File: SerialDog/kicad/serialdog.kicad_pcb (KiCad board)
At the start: 2 copper layers, 4 parts, among them J1 Connector:USB_C_Receptacle, U1 SP0503BAHT, U2 Interface_USB:CP2102N-A01-GQF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

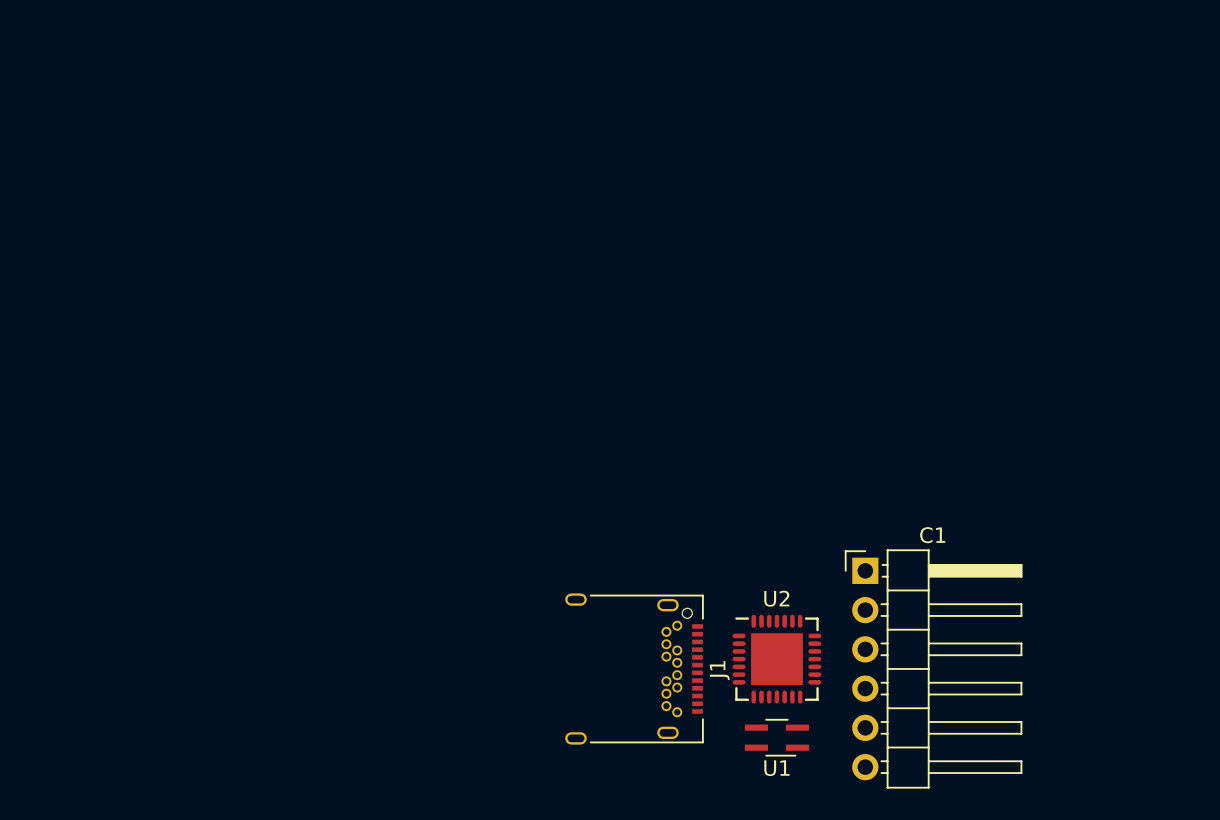
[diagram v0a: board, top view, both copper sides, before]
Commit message: Kicad v5, pcb design started
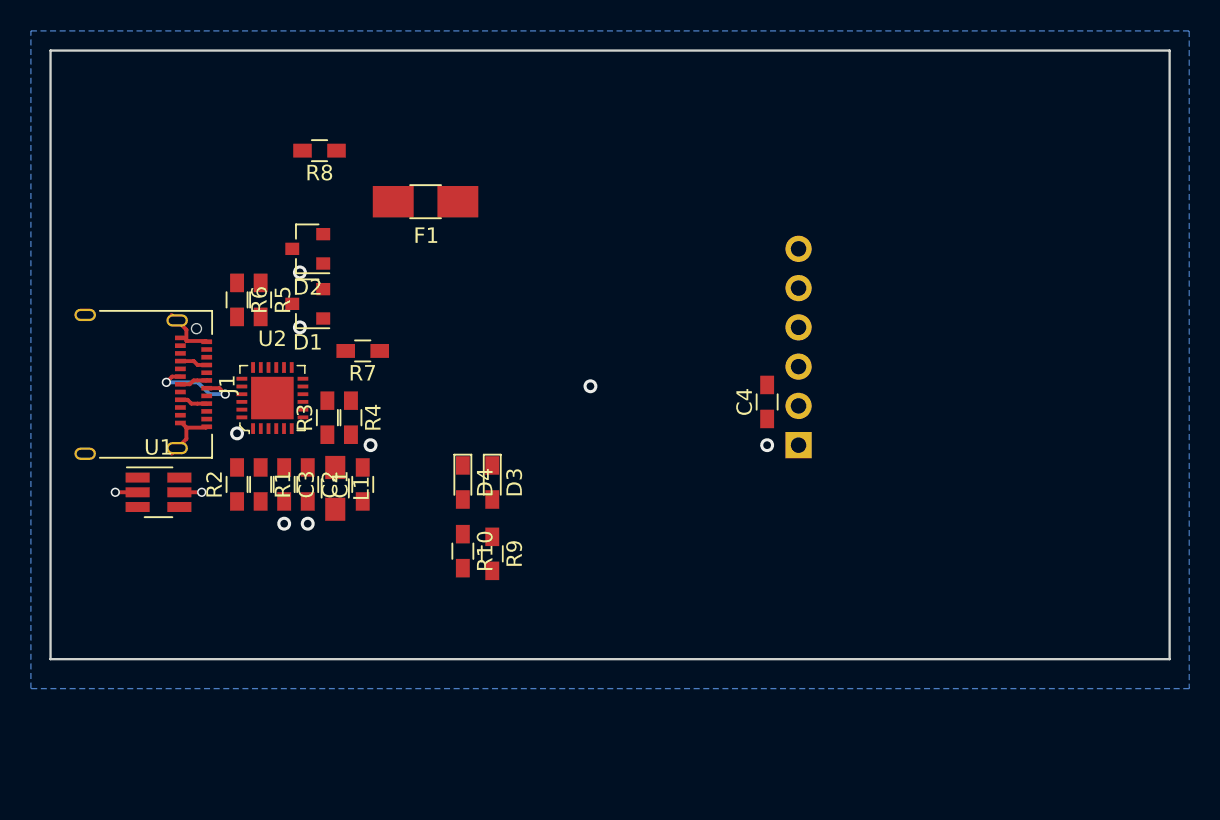
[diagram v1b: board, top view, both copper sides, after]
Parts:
- added C2: 1u, Resistors_SMD:R_0603_HandSoldering, F.Cu at (126.5, 94.7)
- added C3: 1u, Resistors_SMD:R_0603_HandSoldering, F.Cu at (125.0, 94.7)
- added C4: 1u, Resistors_SMD:R_0603_HandSoldering, F.Cu at (156.2, 89.4)
- added D1: BAT54S, TO_SOT_Packages_SMD:SOT-23, F.Cu at (126.5, 83.1)
- added D2: BAT54S, TO_SOT_Packages_SMD:SOT-23, F.Cu at (126.5, 79.5)
- added D3: LED, LEDs:LED_0603_HandSoldering, F.Cu at (138.4, 94.6)
- added D4: LED, LEDs:LED_0603_HandSoldering, F.Cu at (136.5, 94.6)
- added F1: Polyfuse_Small, Fuse_Holders_and_Fuses:Fuse_SMD1206_HandSoldering, F.Cu at (134.1, 76.5)
- added J2: 1x6_2.54_smd_header, Pin_Headers:Pin_Header_Angled_1x06_Pitch2.54mm, B.Cu at (158.2, 92.2)
- added L1: Ferrite_Bead, Resistors_SMD:R_0805_HandSoldering, F.Cu at (128.3, 95.0)
- added R1: 22, Resistors_SMD:R_0603_HandSoldering, F.Cu at (123.4, 94.7)
- added R10: 1k, Resistors_SMD:R_0603_HandSoldering, F.Cu at (136.5, 99.1)
- added R2: 22, Resistors_SMD:R_0603_HandSoldering, F.Cu at (121.9, 94.7)
- added R3: 22k, Resistors_SMD:R_0603_HandSoldering, F.Cu at (127.8, 90.4)
- added R4: 47k, Resistors_SMD:R_0603_HandSoldering, F.Cu at (129.3, 90.4)
- added R5: 22, Resistors_SMD:R_0603_HandSoldering, F.Cu at (123.4, 82.8)
- added R6: 22, Resistors_SMD:R_0603_HandSoldering, F.Cu at (121.9, 82.8)
- added R7: 22, Resistors_SMD:R_0603_HandSoldering, F.Cu at (130.0, 86.1)
- added R8: 22, Resistors_SMD:R_0603_HandSoldering, F.Cu at (127.3, 73.2)
- added R9: 1k, Resistors_SMD:R_0603_HandSoldering, F.Cu at (138.4, 99.2)
- C1: value 1x6_2.54_smd_header -> 1u; footprint Pin_Headers:Pin_Header_Angled_1x06_Pitch2.54mm -> Resistors_SMD:R_0603_HandSoldering
- J1: footprint Connectors_USB:USB_C_Receptacle_Amphenol_12401548E4-2A -> digikey-footprints:USB_C_Receptacle_Amphenol_12401610E4-2A
- U1: value SP0503BAHT -> USBLC6-2SC6; footprint TO_SOT_Packages_SMD:SOT-343_SC-70-4_Handsoldering -> TO_SOT_Packages_SMD:SOT-23-6_Handsoldering
- U2: footprint Housings_DFN_QFN:QFN-28-1EP_5x5mm_Pitch0.5mm -> digikey-footprints:WQFN-24-1EP_4x4mm
- moved U1 43.0 mm to (116.8, 95.2), turned to 0 degrees
- moved U2 36.8 mm to (124.2, 89.2)
- moved J1 36.7 mm to (114.9, 88.3)
- moved C1 33.0 mm to (130.0, 94.7), turned to 90 degrees
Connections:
- C1 pad 1: GND -> /VBUS
- C1 pad 2: Net-(C1-Pad2) -> GND
- J1 pad A4: VCC -> /VBUS
- J1 pad A9: VCC -> /VBUS
- J1 pad B4: VCC -> /VBUS
- J1 pad B6: Net-(J1-PadB6) -> Net-(J1-PadA6)
- J1 pad B7: Net-(J1-PadB7) -> Net-(J1-PadA7)
- J1 pad B9: VCC -> /VBUS
- U1 pad 1: VCC -> Net-(J1-PadA6)
- U1 pad 2: Net-(J1-PadA6) -> GND
- U1 pad 3: Net-(J1-PadB7) -> Net-(J1-PadA7)
- U1 pad 4: GND -> Net-(R1-Pad2)
- U2 pad 20: Net-(C1-Pad4) -> Net-(R5-Pad2)
- U2 pad 21: Net-(C1-Pad5) -> Net-(R6-Pad2)
- U2 pad 3: Net-(J1-PadA6) -> Net-(R2-Pad2)
- U2 pad 4: Net-(J1-PadB7) -> Net-(R1-Pad1)
- U2 pad 5: VCC -> Net-(C3-Pad1)
- U2 pad 6: VCC -> Net-(C3-Pad1)
- U2 pad 7: Net-(U2-Pad7) -> /REGIN
- U2 pad 8: VCC -> Net-(R3-Pad2)
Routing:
- net GND: track 0.00 -> 8.79 mm, vias 0 -> 9
- net Net-(J1-PadA7): track 0.00 -> 6.55 mm, vias 0 -> 2
- net /VBUS: track 0.00 -> 5.05 mm, vias 0 -> 1
- net Net-(J1-PadA6): track 0.00 -> 1.84 mm
- added copper zone on B.Cu, net GND
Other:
- board outline added: 72.4 x 39.4 mm

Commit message: Made first pcb layout draft
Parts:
- C3: footprint Resistors_SMD:R_0603_HandSoldering -> Capacitors_SMD:C_0805
- D3, D4: footprint LEDs:LED_0603_HandSoldering -> LEDs:LED_0603
- J2: footprint Pin_Headers:Pin_Header_Angled_1x06_Pitch2.54mm -> uart-adapters:1x6 header female smd; moved to F.Cu
- R1, R10, R2, R3, R4, R5, R6, R7, R8, R9: footprint Resistors_SMD:R_0603_HandSoldering -> Resistors_SMD:R_0603
- moved C4 23.0 mm to (133.6, 85.0), turned to 0 degrees
- moved J2 21.1 mm to (137.2, 92.5)
- moved R9 14.4 mm to (129.0, 88.3), turned to 180 degrees
- moved R8 13.5 mm to (130.4, 86.2)
- moved F1 13.2 mm to (134.5, 89.7), turned to 90 degrees
- moved R10 12.1 mm to (129.0, 89.5), turned to 180 degrees
- moved D3 9.25 mm to (131.7, 88.3), turned to 180 degrees
- moved J1 8.13 mm to (122.0, 92.2)
- moved U2 7.30 mm to (130.4, 93.0)
- moved R3 7.19 mm to (133.6, 94.6)
- moved D4 7.01 mm to (131.7, 89.5), turned to 180 degrees
- moved R4 6.98 mm to (134.9, 94.6)
- moved D2 6.67 mm to (124.1, 85.7), turned to 0 degrees
- moved C2 6.67 mm to (130.8, 99.8), turned to 180 degrees
- moved C1 6.45 mm to (135.3, 98.6)
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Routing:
- net /VBUS: track 5.05 -> 31.4 mm, vias 1 -> 4
- net Net-(C3-Pad1): track 0.00 -> 20.9 mm, vias 0 -> 4
- net GND: track 8.79 -> 28.1 mm, vias 9 -> 6
- net Net-(R6-Pad2): track 0.00 -> 17.4 mm, vias 0 -> 2
- net /REGIN: track 0.00 -> 16.7 mm, vias 0 -> 2
- net Net-(J2-Pad4): track 0.00 -> 16.6 mm, vias 0 -> 2
- net Net-(J2-Pad5): track 0.00 -> 15.3 mm, vias 0 -> 2
- net Net-(R5-Pad2): track 0.00 -> 14.0 mm, vias 0 -> 2
- net /VOUT: track 0.00 -> 13.1 mm
- net Net-(J1-PadA7): track 6.55 -> 15.0 mm, vias 2 -> 3
- net /TX: track 0.00 -> 8.41 mm
- net Net-(J1-PadA6): track 1.84 -> 10.2 mm
- net /RX: track 0.00 -> 7.73 mm, vias 0 -> 2
- net Net-(R2-Pad2): track 0.00 -> 6.61 mm
- net Net-(R1-Pad1): track 0.00 -> 6.08 mm
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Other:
- board size 72.4 x 39.4 mm -> 30 x 16.5 mm
